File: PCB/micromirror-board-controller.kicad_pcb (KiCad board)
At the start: 2 copper layers, 65 x 35 mm, 24 parts, among them J1 RPi header, J2 DMD board PWR, J3 Conn_01x03_Female, J4 51-pin conn, J5 Barrel_Jack, J6 Extra GPIO, J7 5V Ext, J8 STEMMA, U2 CUI P78E05-1000

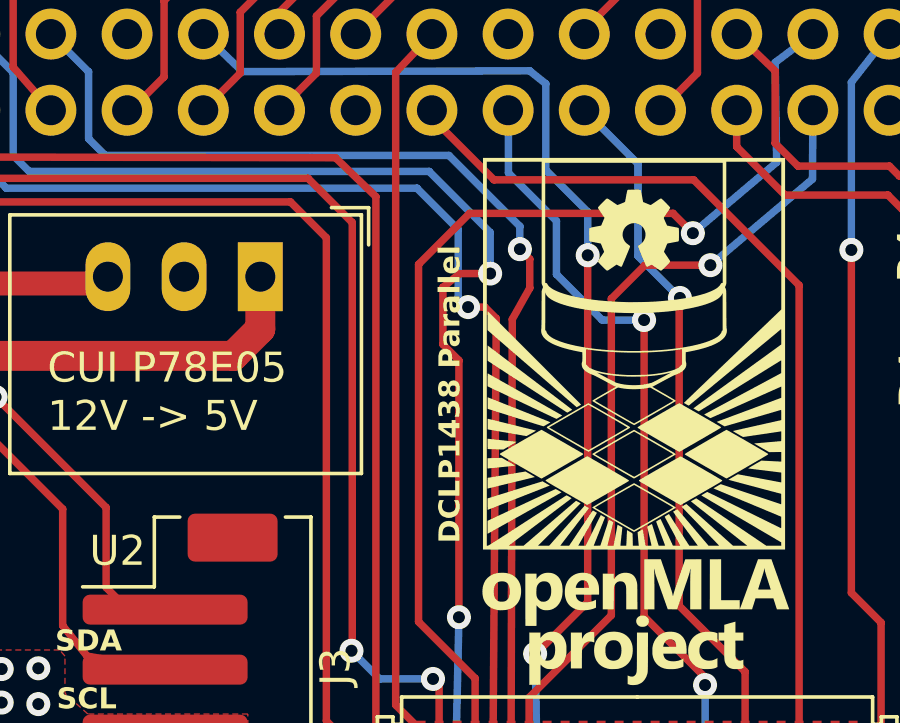
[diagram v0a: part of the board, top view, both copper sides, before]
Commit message: fix silkscreen error
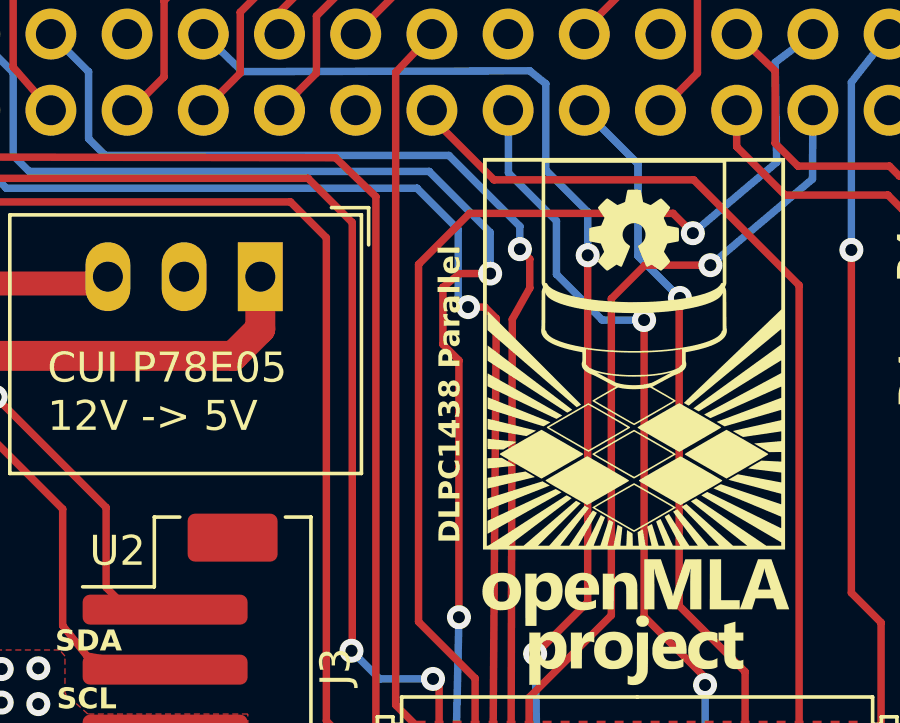
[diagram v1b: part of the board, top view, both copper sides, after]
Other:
- board text added: "DLPC1438 Parallel"
- board text removed: "DCLP1438 Parallel"
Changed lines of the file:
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@@
     (effects (font (size 1 1) (thickness 0.15)) (justify left bottom mirror))
   )
-  (gr_text "DCLP1438 Parallel" (at 142.3924 89.2048 90) (layer "F.SilkS" knockout)
+  (gr_text "DLPC1438 Parallel" (at 142.3924 89.2048 90) (layer "F.SilkS" knockout)
     (effects (font (size 0.7 0.7) (thickness 0.12) bold) (justify left bottom))
   )

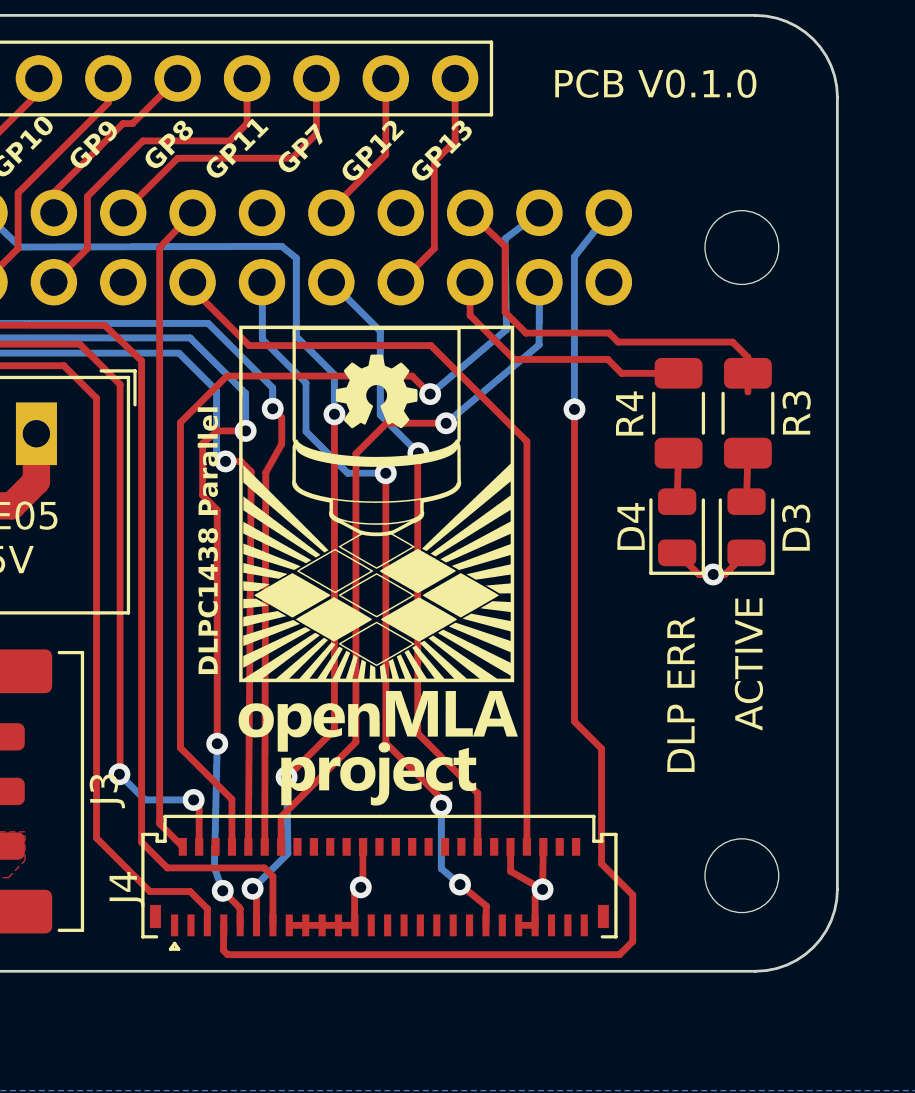
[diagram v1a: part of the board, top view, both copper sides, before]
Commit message: Fix incorrect pinout for pixeldata
Corrected the incorrect pinout of the pixeldata section of the FPC connector. Even and odd pins had to be switched (P0 <-> P1) etc. Fixes https://github.com/openMLA/photon-ultra-controller/issues/2.
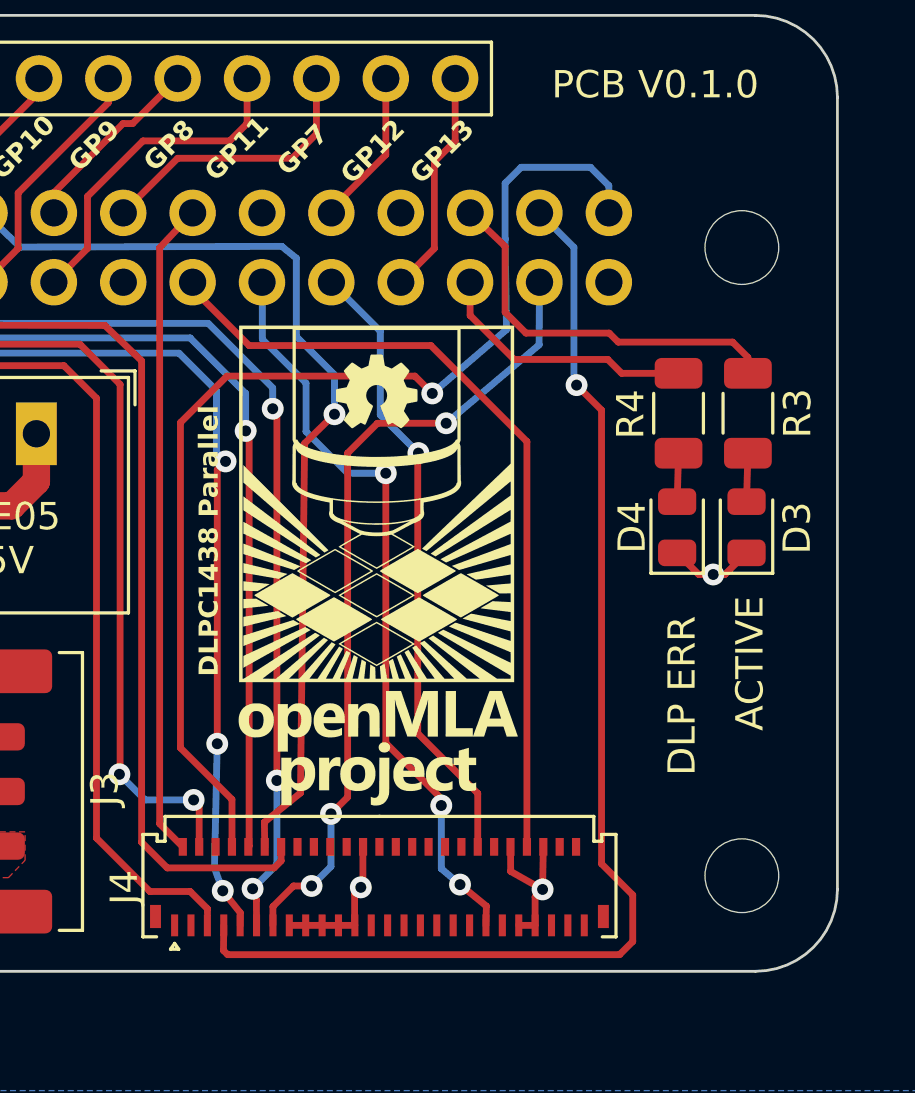
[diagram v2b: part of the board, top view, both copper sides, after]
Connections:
- J4 pad 10: P2 -> P3
- J4 pad 11: P5 -> P4
- J4 pad 12: P4 -> P5
- J4 pad 13: P7 -> P6
- J4 pad 14: P6 -> P7
- J4 pad 7: P1 -> P0
- J4 pad 8: P0 -> P1
- J4 pad 9: P3 -> P2
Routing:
- net P0: track 35.0 -> 44.3 mm
- net P3: track 42.8 -> 38.2 mm, vias 3 -> 1
- net P6: track 26.0 -> 29.6 mm, vias 1 -> 3
- net P1: track 44.2 -> 40.8 mm
- net P5: track 38.4 -> 35.3 mm, vias 3 -> 1
- net P4: track 36.7 -> 39.7 mm, vias 1 -> 3
- net P2: track 36.2 -> 38.8 mm, vias 1 -> 3
- net P7: track 42.0 -> 41.0 mm
- net LED-G: track 15.0 -> 14.3 mm

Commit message: Move barrel jack slightly for enclosure purposes
Moved the DC barrel jack on the PCB to facilitate the design of enclosures. The Connector now sticks out from the PCB board edge, allowing a 3D printed enclosure or similar to allow flush access to the connector.
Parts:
- moved J5 3.00 mm to (111.0, 86.1)
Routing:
- net GND: track 30.7 -> 33.1 mm
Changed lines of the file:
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@@
   )
   (footprint "Connector_BarrelJack:BarrelJack_GCT_DCJ200-10-A_Horizontal" (layer "F.Cu")
-    (at 114.0252 86.0814 -90)
+    (at 111.0252 86.0814 -90)
     (descr "Barrel jack connector (5.5 mm outer diameter, 2.05 inner diameter ), https://gct.co/files/drawings/dcj200-10.pdf")
     (tags "connector barrel jack")
@@
     (effects (font (size 0.7 0.7) (thickness 0.12) bold) (justify left bottom))
   )
-  (gr_text "Center Positive\n5.5 : 2.5mm" (at 100.5332 93.0656) (layer "F.SilkS")
+  (gr_text "Center Positive\n5.5 : 2.5mm" (at 114.554 90.0176 90) (layer "F.SilkS")
     (effects (font (size 0.7 0.7) (thickness 0.12) bold) (justify left bottom))
   )
@@
     (effects (font (size 0.7 0.7) (thickness 0.12) bold) (justify left bottom))
   )
-  (gr_text "12V in" (at 116.4336 87.7316 90) (layer "F.SilkS" knockout)
+  (gr_text "12V in" (at 116.2812 87.9348 90) (layer "F.SilkS" knockout)
     (effects (font (size 0.7 0.7) (thickness 0.12) bold) (justify left bottom))
   )
@@
   (segment (start 153.0352 96.3424) (end 154.2036 97.0028) (width 0.25) (layer "F.Cu") (net 1))
   (segment (start 147.3202 98.3082) (end 147.3304 98.3184) (width 0.25) (layer "F.Cu") (net 1))
-  (segment (start 109.332 94.9302) (end 109.332 96.1138) (width 1.5) (layer "F.Cu") (net 1))
   (segment (start 107.7252 93.3234) (end 109.332 94.9302) (width 1.5) (layer "F.Cu") (net 1))
   (segment (start 160.452 85.471) (end 160.879 85.471) (width 0.25) (layer "F.Cu") (net 1))
   (segment (start 147.3202 97.1552) (end 147.3202 98.3082) (width 0.25) (layer "F.Cu") (net 1))
   (segment (start 147.624441 96.850959) (end 147.5488 96.9266) (width 0.25) (layer "F.Cu") (net 1))
-  (segment (start 107.7252 86.0814) (end 107.7252 93.3234) (width 1.5) (layer "F.Cu") (net 1))
   (segment (start 153.9304 97.276) (end 154.2036 97.0028) (width 0.25) (layer "F.Cu") (net 1))
   (segment (start 154.2304 95.4434) (end 154.2036 97.0028) (width 0.25) (layer "F.Cu") (net 1))
+  (segment (start 104.7252 92.2284) (end 105.8202 93.3234) (width 1.5) (layer "F.Cu") (net 1))
   (segment (start 160.879 85.471) (end 161.671 84.679) (width 0.25) (layer "F.Cu") (net 1))
+  (segment (start 104.7252 86.0814) (end 104.7252 92.2284) (width 1.5) (layer "F.Cu") (net 1))
   (segment (start 153.9304 98.3184) (end 153.9304 97.276) (width 0.25) (layer "F.Cu") (net 1))
   (segment (start 153.3304 98.3184) (end 153.9304 98.3184) (width 0.25) (layer "F.Cu") (net 1))
@@
   (segment (start 159.923 85.471) (end 159.131 84.679) (width 0.25) (layer "F.Cu") (net 1))
   (segment (start 147.5488 96.9266) (end 147.3202 97.1552) (width 0.25) (layer "F.Cu") (net 1))
+  (segment (start 105.8202 93.3234) (end 107.7252 93.3234) (width 1.5) (layer "F.Cu") (net 1))
   (segment (start 147.624441 95.449359) (end 147.624441 96.850959) (width 0.25) (layer "F.Cu") (net 1))
   (segment (start 147.6304 95.4434) (end 147.624441 95.449359) (width 0.25) (layer "F.Cu") (net 1))
+  (segment (start 109.332 94.9302) (end 109.332 96.1138) (width 1.5) (layer "F.Cu") (net 1))
   (via (at 128.2702 94.5644) (size 0.8) (drill 0.4) (layers "F.Cu" "B.Cu") (free) (net 1))
   (via (at 128.2702 95.682) (size 0.8) (drill 0.4) (layers "F.Cu" "B.Cu") (free) (net 1))
@@
     (polygon
       (pts
-        (xy 113.0302 83.6678)
-        (xy 113.0556 88.4176)
-        (xy 114.1986 89.459)
-        (xy 114.1986 93.5484)
-        (xy 112.9794 94.539)
+        (xy 109.474 83.6168)
+        (xy 109.474 88.5952)
+        (xy 112.9792 91.3384)
         (xy 112.9794 96.9012)
         (xy 116.4846 96.9266)
@@
         (xy 121.7678 84.2266)
         (xy 121.7678 81.7628)
-        (xy 114.859 81.7628)
+        (xy 111.0488 81.788)
       )
     )
